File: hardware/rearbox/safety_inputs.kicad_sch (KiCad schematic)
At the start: 9 parts, among them U9 TCA6416ARTWR

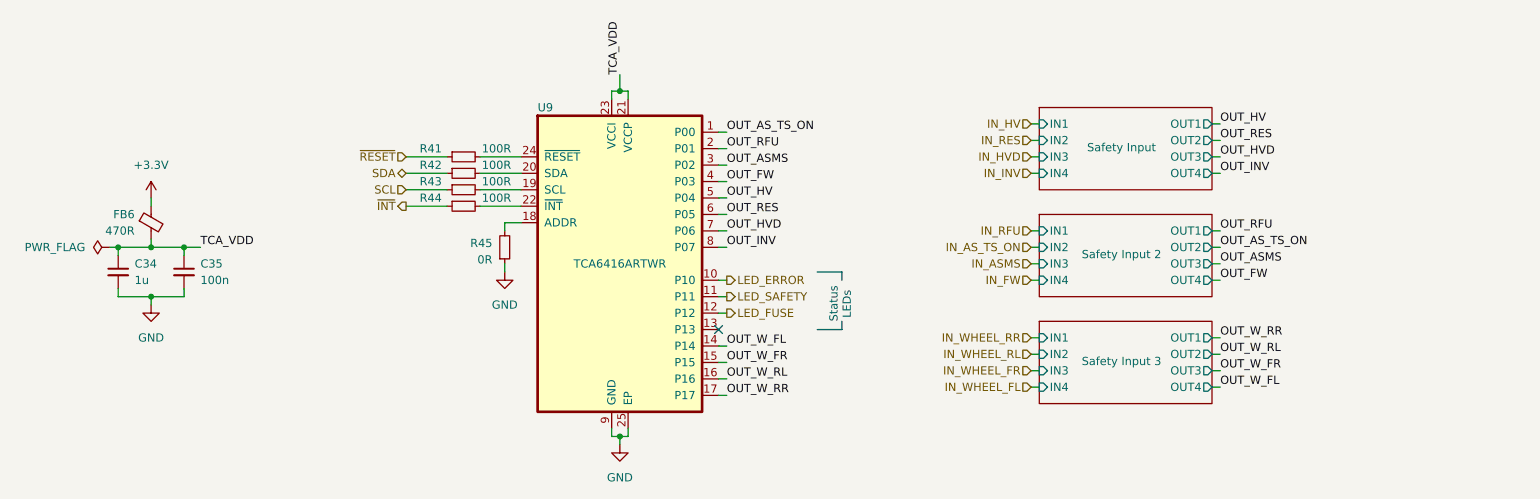
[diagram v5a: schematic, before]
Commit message: Fix measurement bridges polarity
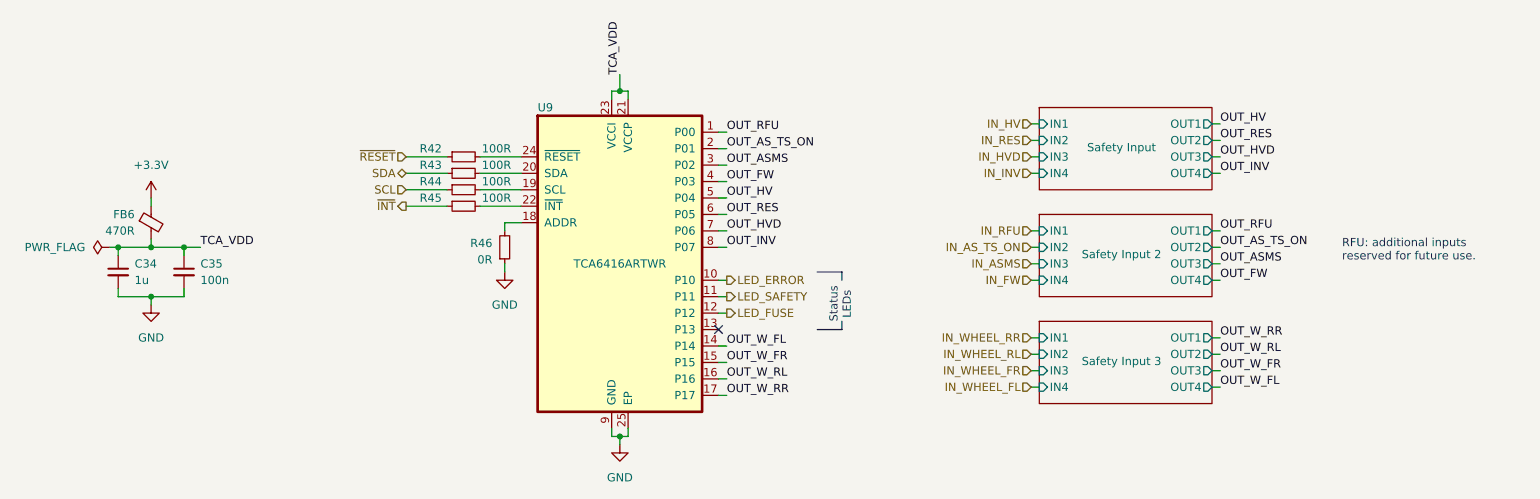
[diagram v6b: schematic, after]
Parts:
- renumbered R41 to R42, R42 to R43, R43 to R44, R44 to R45, R45 to R46
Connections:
- net OUT_AS_TS_ON: now also U9.2 (P01); no longer U9.1 (P00)
- net OUT_RFU: now also U9.1 (P00); no longer U9.2 (P01)
